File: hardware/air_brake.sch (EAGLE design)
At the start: 20 parts

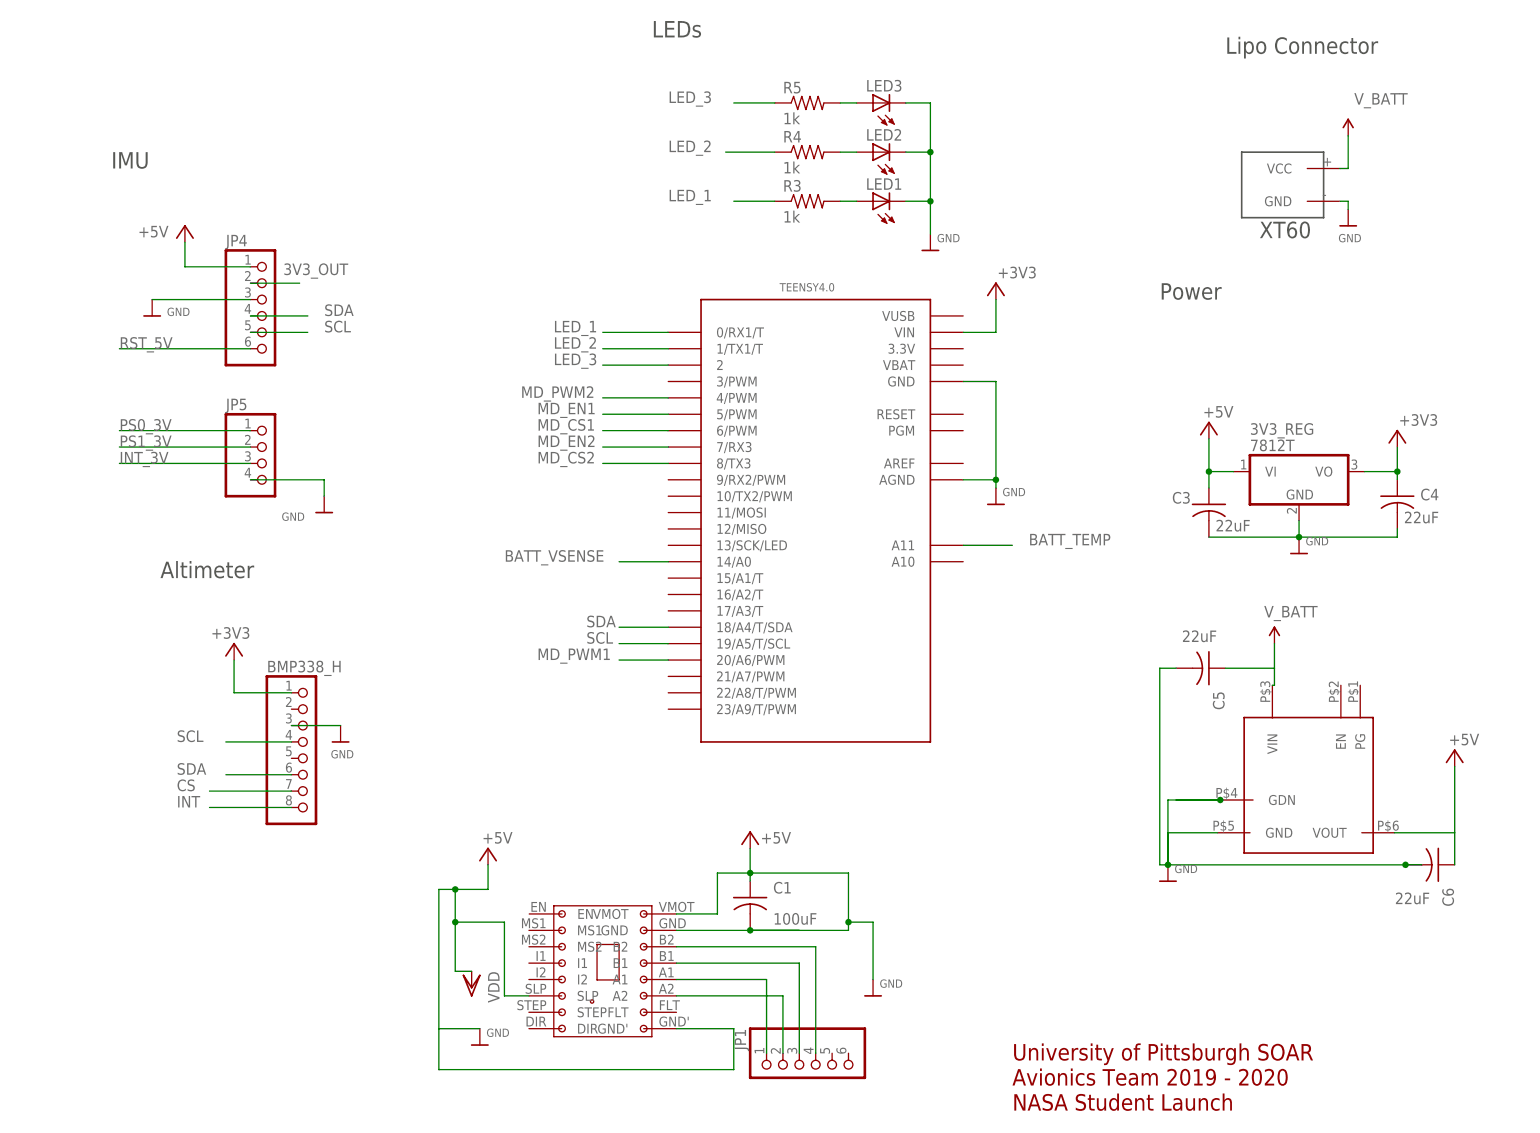
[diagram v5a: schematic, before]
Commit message: Changed to Teensy 3.6
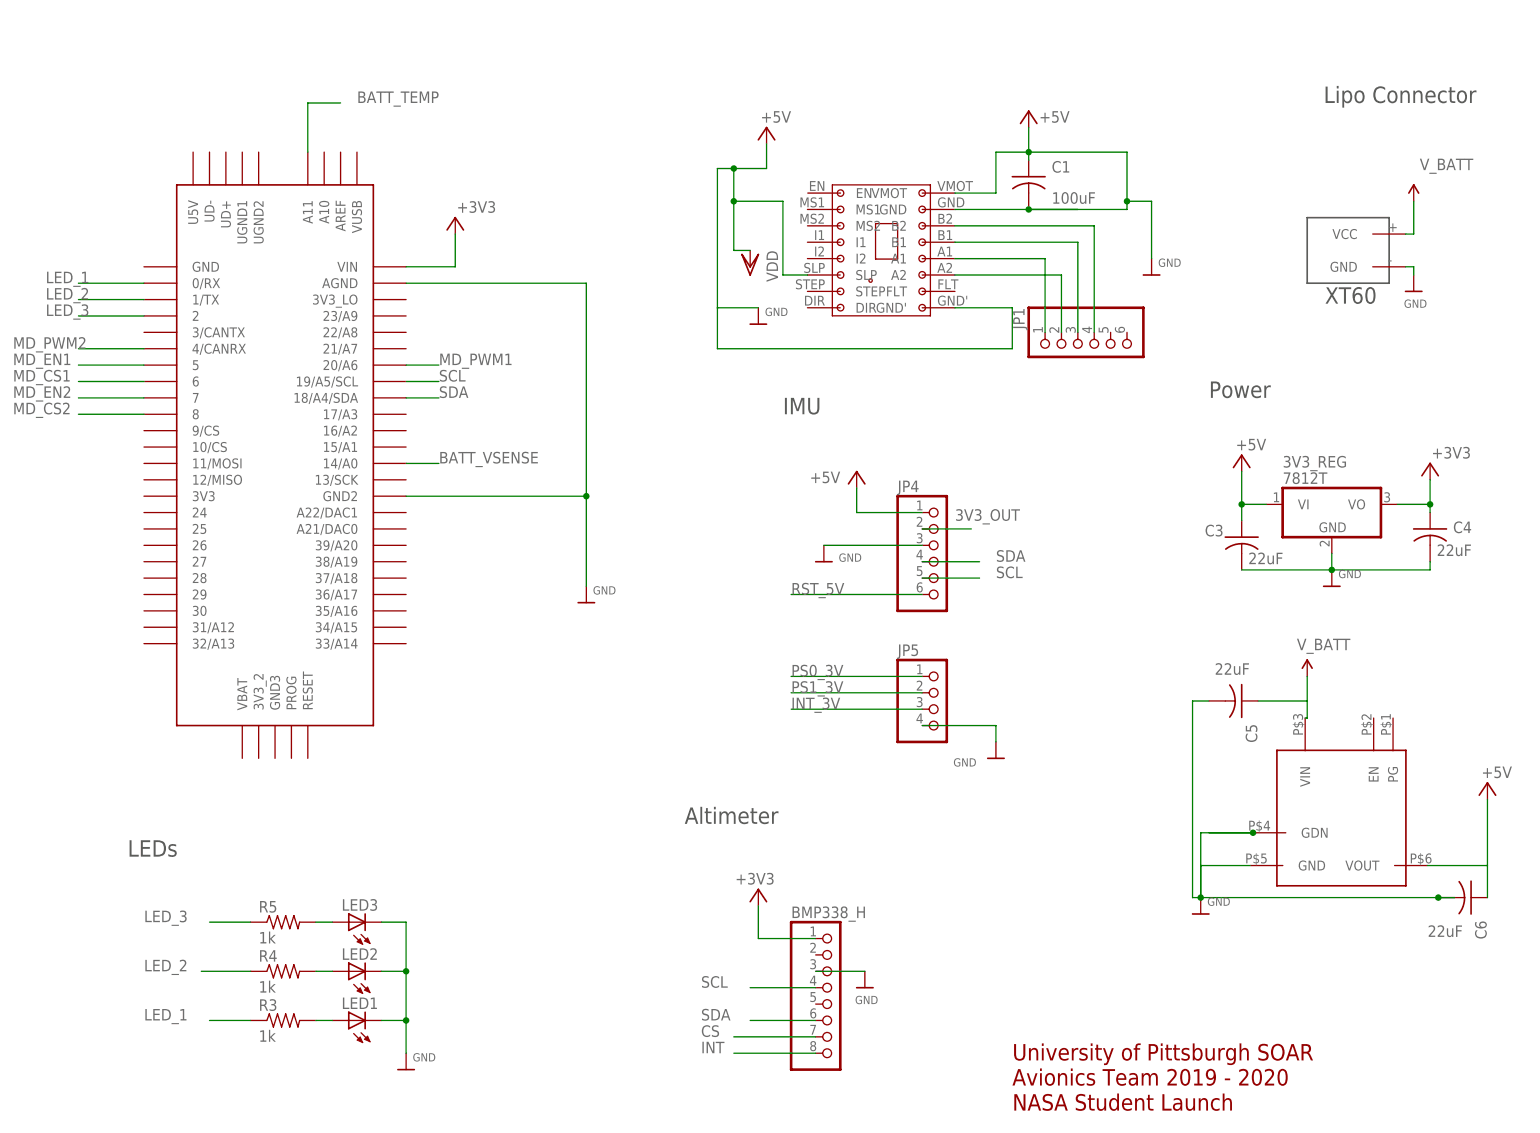
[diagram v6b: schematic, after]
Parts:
- removed TEENSY4.0: TEENSY_3.0_ALL_PINS, Teensy_3_and_LC_Series_Boards_v1.4:TEENSY_3.0_ALL_PINS
- added U$14: TEENSY_3.5/3.6, Teensy356:TEENSY_3.5/3.6
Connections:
- net +3V3: now also U$14.VIN; no longer TEENSY4.0.VIN
- net BATT_TEMP: now also U$14.A11; no longer TEENSY4.0.A11
- net BATT_VSENSE: now also U$14.14/A0; no longer TEENSY4.0.14/A0
- net GND: now also U$14.AGND, U$14.GND2; no longer TEENSY4.0.AGND, TEENSY4.0.GND
- net LED_1: now also U$14.0/RX; no longer TEENSY4.0.0/RX1/T
- net LED_2: now also U$14.1/TX; no longer TEENSY4.0.1/TX1/T
- net LED_3: now also U$14.2; no longer TEENSY4.0.2
- net MD_CS1: now also U$14.6; no longer TEENSY4.0.6/PWM
- net MD_CS2: now also U$14.8; no longer TEENSY4.0.8/TX3
- net MD_EN1: now also U$14.5; no longer TEENSY4.0.5/PWM
- net MD_EN2: now also U$14.7; no longer TEENSY4.0.7/RX3
- net MD_PWM1: now also U$14.20/A6; no longer TEENSY4.0.20/A6/PWM
- net MD_PWM2: now also U$14.4/CANRX; no longer TEENSY4.0.4/PWM
- net SCL: now also U$14.19/A5/SCL; no longer TEENSY4.0.19/A5/T/SCL
- net SDA: now also U$14.18/A4/SDA; no longer TEENSY4.0.18/A4/T/SDA
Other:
- moved on the sheet: 3V3_REG, BMP338_H, C1, C3, C4, C5, C6, JP1, JP4, JP5, LED1, LED2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

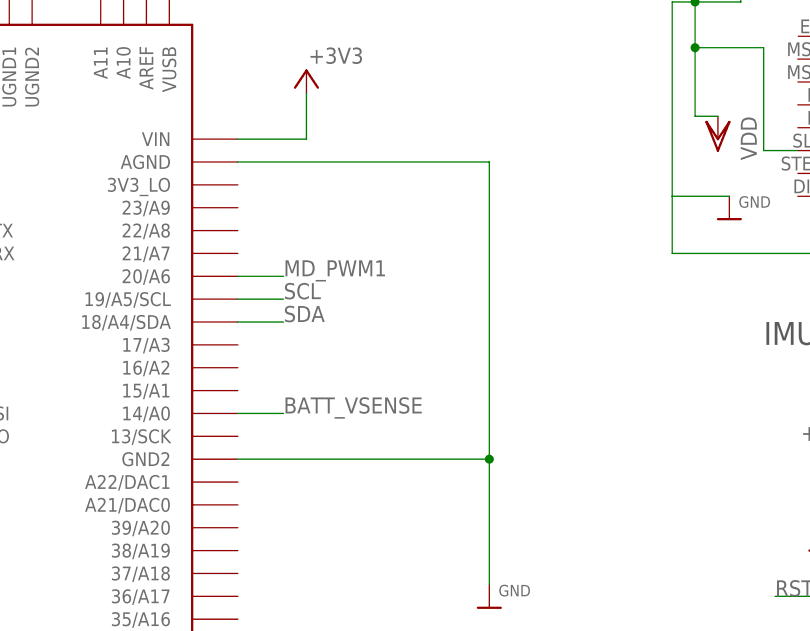
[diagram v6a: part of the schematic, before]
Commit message: Added Buzzer
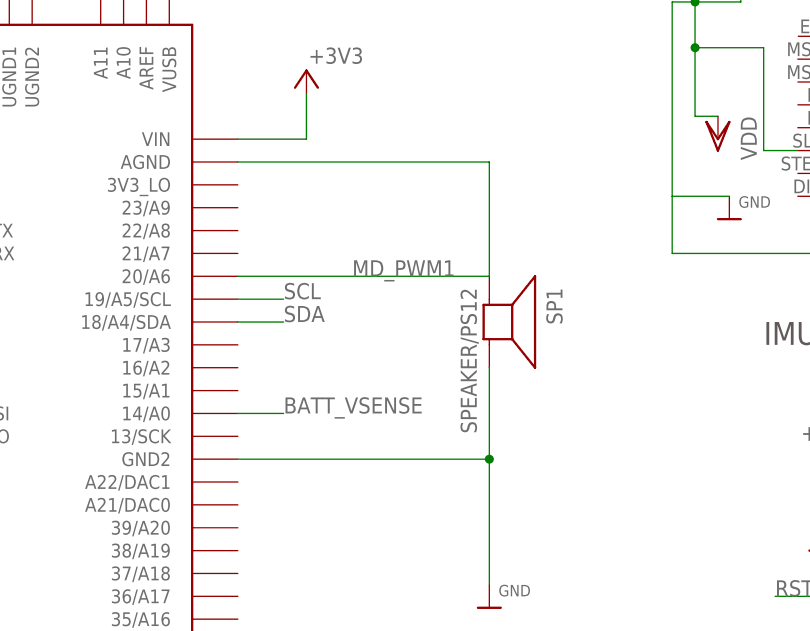
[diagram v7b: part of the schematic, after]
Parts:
- added SP1: SPEAKER/PS12, adafruit:SPEAKER/PS12
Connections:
- net GND: now also SP1.-; no longer U$14.AGND
- net MD_PWM1: now also SP1.+, U$14.AGND
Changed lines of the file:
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@@
 <part name="+3V4" library="supply1" deviceset="+3V3" device=""/>
 <part name="U$15" library="microbuilder" deviceset="GND" device=""/>
+<part name="SP1" library="adafruit" deviceset="SPEAKER" device="/PS12"/>
 </parts>
 <sheets>
@@
 <attribute name="VALUE" x="100.076" y="86.36" size="1.27" layer="96"/>
 </instance>
+<instance part="SP1" gate="S1" x="99.06" y="116.84" smashed="yes" rot="R270">
+<attribute name="NAME" x="105.41" y="120.65" size="1.778" layer="95" rot="R270"/>
+<attribute name="VALUE" x="95.885" y="120.65" size="1.778" layer="96" rot="R270"/>
+</instance>
 </instances>
 <busses>
@@
 </segment>
 <segment>
-<pinref part="U$14" gate="G$1" pin="AGND"/>
-<wire x1="71.12" y1="134.62" x2="99.06" y2="134.62" width="0.1524" layer="91" grouprefs="TEENSY3.6"/>
-<wire x1="99.06" y1="134.62" x2="99.06" y2="101.6" width="0.1524" layer="91" grouprefs="TEENSY3.6"/>
 <pinref part="U$14" gate="G$1" pin="GND2"/>
 <wire x1="99.06" y1="101.6" x2="99.06" y2="87.63" width="0.1524" layer="91" grouprefs="TEENSY3.6"/>
@@
 <junction x="99.06" y="101.6" grouprefs="TEENSY3.6"/>
 <pinref part="U$15" gate="G$1" pin="GND"/>
+<wire x1="99.06" y1="111.76" x2="99.06" y2="101.6" width="0.1524" layer="91" grouprefs="TEENSY3.6"/>
+<pinref part="SP1" gate="S1" pin="-"/>
 </segment>
 </net>
@@
 <segment>
 <pinref part="U$14" gate="G$1" pin="18/A4/SDA"/>
-<wire x1="71.12" y1="116.84" x2="76.2" y2="116.84" width="0.1524" layer="91" grouprefs="TEENSY3.6 TEENSY3.6"/>
+<wire x1="71.12" y1="116.84" x2="76.2" y2="116.84" width="0.1524" layer="91" grouprefs="TEENSY3.6"/>
 <label x="76.2" y="116.84" size="1.778" layer="95" grouprefs="TEENSY3.6"/>
 </segment>
@@
 <segment>
 <pinref part="U$14" gate="G$1" pin="19/A5/SCL"/>
-<wire x1="71.12" y1="119.38" x2="76.2" y2="119.38" width="0.1524" layer="91" grouprefs="TEENSY3.6 TEENSY3.6"/>
+<wire x1="71.12" y1="119.38" x2="76.2" y2="119.38" width="0.1524" layer="91" grouprefs="TEENSY3.6"/>
 <label x="76.2" y="119.38" size="1.778" layer="95" grouprefs="TEENSY3.6"/>
 </segment>
@@
 <segment>
 <pinref part="U$14" gate="G$1" pin="14/A0"/>
-<wire x1="71.12" y1="106.68" x2="76.2" y2="106.68" width="0.1524" layer="91" grouprefs="TEENSY3.6 TEENSY3.6"/>
+<wire x1="71.12" y1="106.68" x2="76.2" y2="106.68" width="0.1524" layer="91" grouprefs="TEENSY3.6"/>
 <label x="76.2" y="106.68" size="1.778" layer="95" grouprefs="TEENSY3.6"/>
 </segment>
@@
 <segment>
 <pinref part="U$14" gate="G$1" pin="20/A6"/>
-<wire x1="71.12" y1="121.92" x2="76.2" y2="121.92" width="0.1524" layer="91" grouprefs="TEENSY3.6 TEENSY3.6"/>
-<label x="76.2" y="121.92" size="1.778" layer="95" grouprefs="TEENSY3.6"/>
-</segment>
-</net>
+<label x="83.82" y="121.92" size="1.778" layer="95" grouprefs="TEENSY3.6"/>
+<wire x1="99.06" y1="134.62" x2="99.06" y2="121.92" width="0.1524" layer="91" grouprefs="TEENSY3.6"/>
+<pinref part="U$14" gate="G$1" pin="AGND"/>
+<wire x1="71.12" y1="134.62" x2="99.06" y2="134.62" width="0.1524" layer="91" grouprefs="TEENSY3.6"/>
+<pinref part="SP1" gate="S1" pin="+"/>
+<wire x1="71.12" y1="121.92" x2="99.06" y2="121.92" width="0.1524" layer="91"/>
+</segment>
+</net>
